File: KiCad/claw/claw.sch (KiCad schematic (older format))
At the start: 15 parts, among them J1 Molex_Spox_3pin, J2 Molex_Spox_3pin, J3 Molex_Spox_3pin, J4 Molex_Spox_3pin, J5 Molex_Spox_3pin, J6 Screw_Terminal_01x02, U1 ESP32_DEVKITV1, U2 TXS0108EPW, U3 74LS241

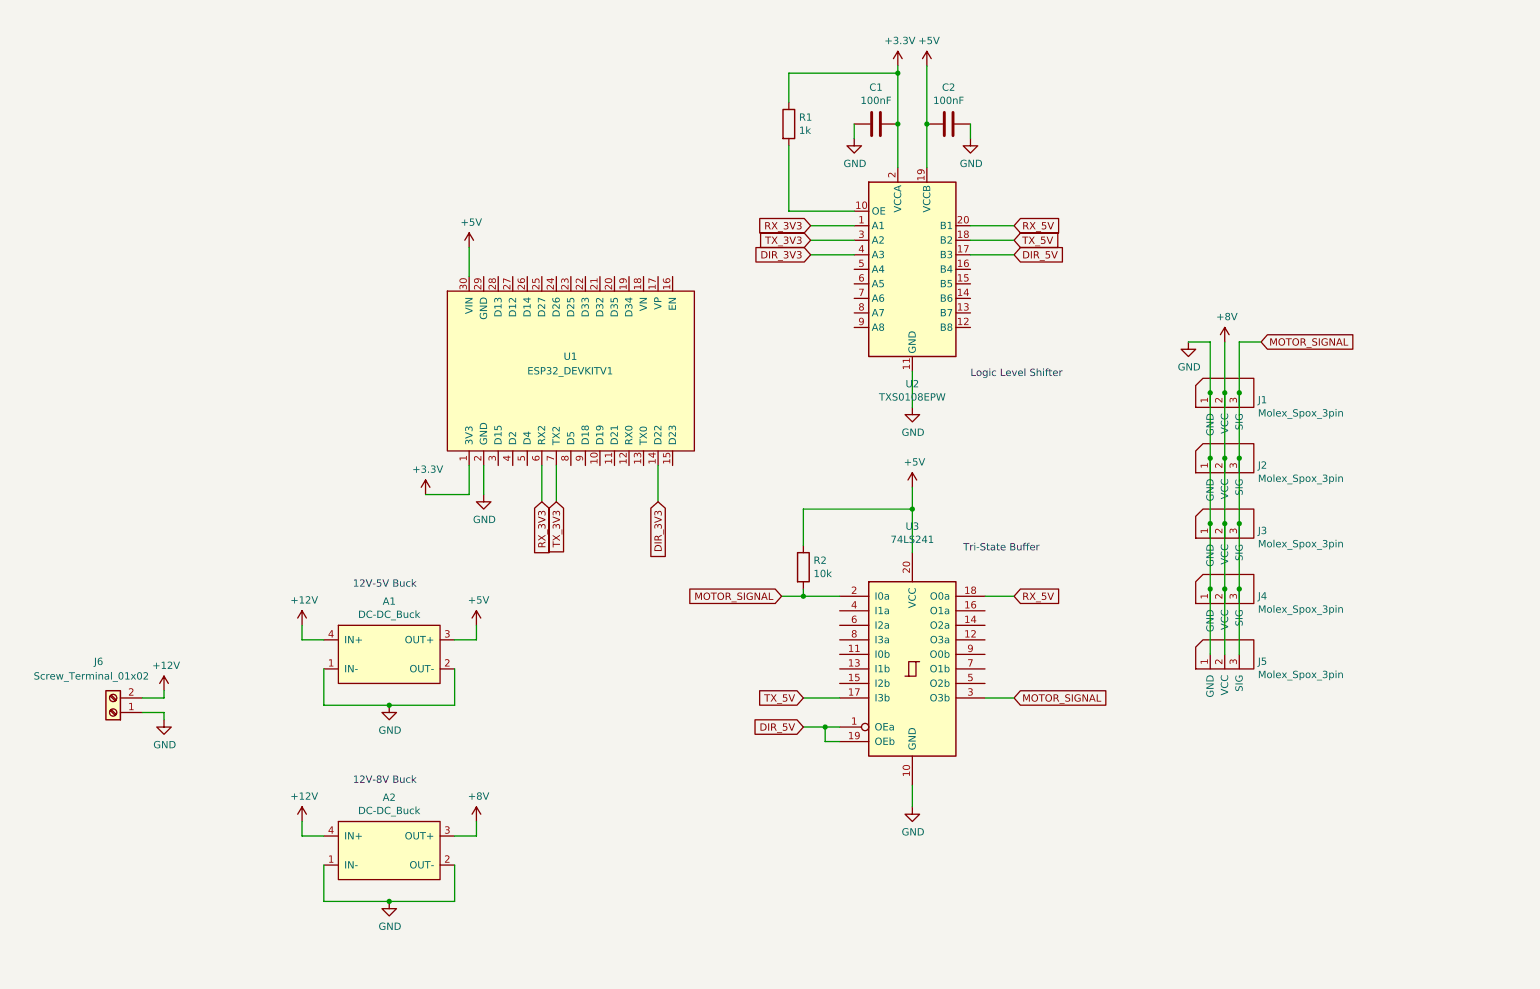
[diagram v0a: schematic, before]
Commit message: added joystick connectors to schematic and layed out components on pcb
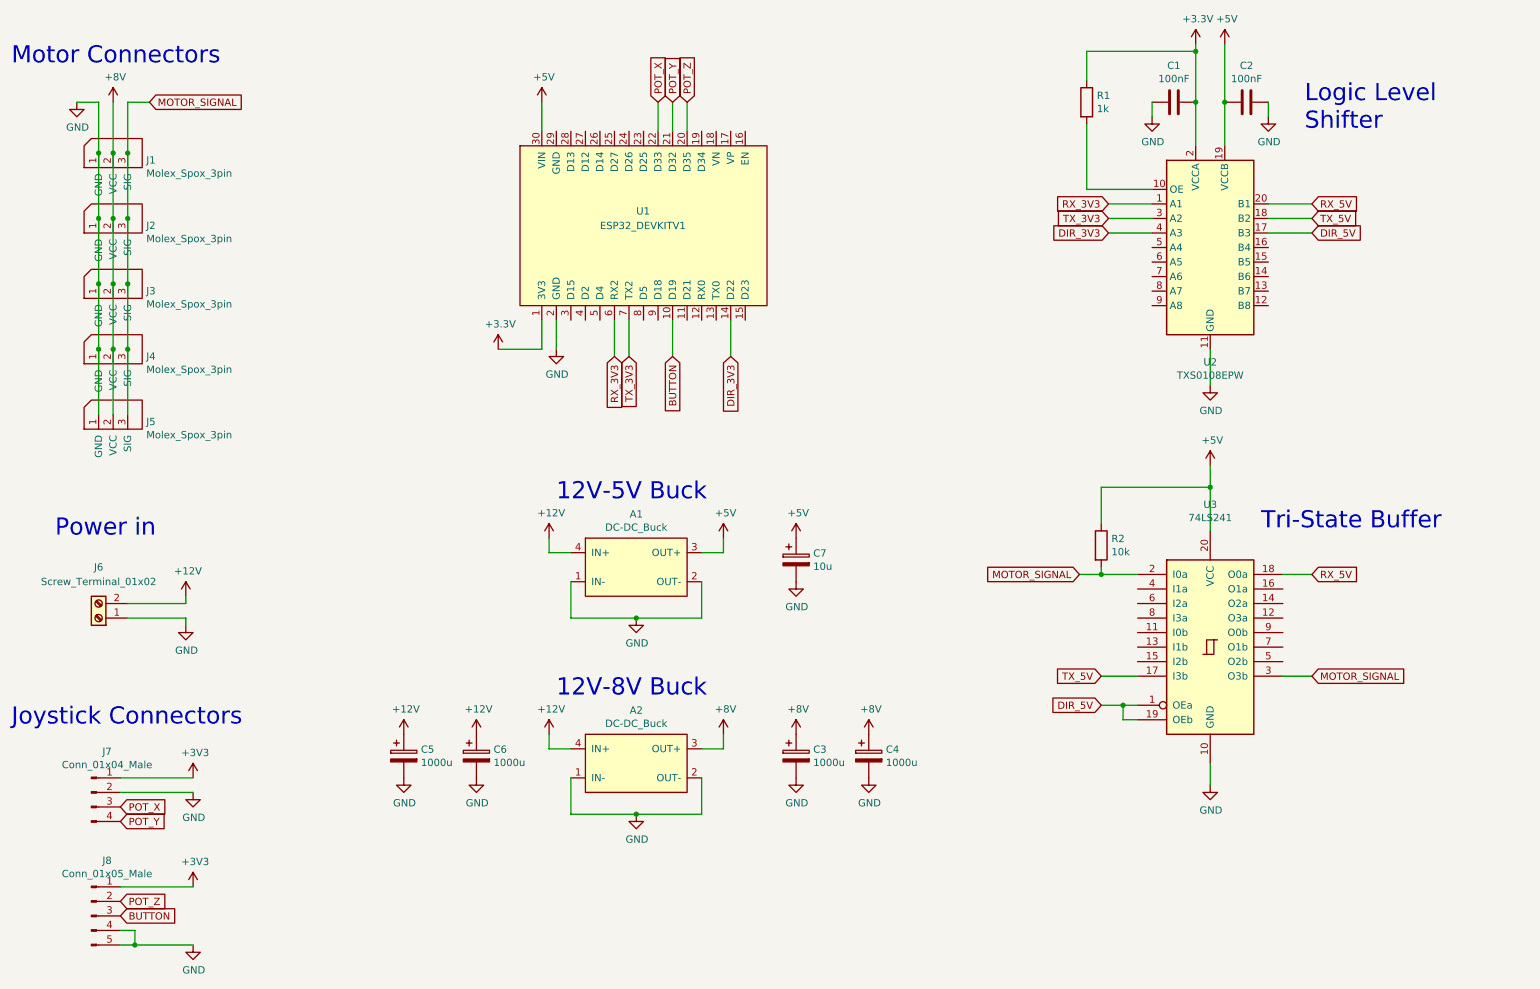
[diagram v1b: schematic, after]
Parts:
- added C3, C4, C5, C6: 1000u, Capacitor_THT:CP_Radial_D10.0mm_P5.00mm, symbol Device:CP
- added C7: 10u, Capacitor_THT:CP_Radial_D4.0mm_P2.00mm, symbol Device:CP
- added J7: Conn_01x04_Male, Connector_JST:JST_PH_B4B-PH-K_1x04_P2.00mm_Vertical, symbol Connector:Conn_01x04_Male
- added J8: Conn_01x05_Male, Connector_JST:JST_PH_B5B-PH-K_1x05_P2.00mm_Vertical, symbol Connector:Conn_01x05_Male
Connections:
- net +12V: now also C5.1, C6.1
- net +3V3: now also J7.1 (Pin_1), J8.1 (Pin_1)
- net +5V: now also C7.1
- net +8V: now also C3.1, C4.1
- net GND: now also C3.2, C4.2, C5.2, C6.2, C7.2, J7.2 (Pin_2), J8.4 (Pin_4), J8.5 (Pin_5)
- net BUTTON: now reaches U1.10 (D19)
- net BUTTON: now also J8.3 (Pin_3)
- net POT_Z: now reaches U1.20 (D35)
- net POT_Z: now also J8.2 (Pin_2)
- net POT_Y: now reaches U1.21 (D32)
- net POT_Y: now also J7.4 (Pin_4)
- net POT_X: now reaches U1.22 (D33)
- net POT_X: now also J7.3 (Pin_3)
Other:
- note added: "Joystick Connectors"
- note added: "Logic Level\nShifter\n"
- note added: "Motor Connectors"
- note added: "Power in"
- note removed: "Logic Level Shifter\n"
- moved on the sheet: A1, A2, C1, C2, J1, J2, J3, J4, J5, J6, R1, R2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

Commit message: pcb traces
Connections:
- net GND: now also U1.29 (GND)
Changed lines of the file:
@@
 Text Notes 1050 4350 0    118  ~ 0
 Power in
+$Comp
+L power:GND #PWR?
+U 1 1 61BD6521
+P 4600 1300
+F 0 "#PWR?" H 4600 1050 50  0001 C CNN
+F 1 "GND" H 4605 1127 50  0000 C CNN
+F 2 "" H 4600 1300 50  0001 C CNN
+F 3 "" H 4600 1300 50  0001 C CNN
+	1    4600 1300
+	1    0    0    -1
+$EndComp
+Wire Wire Line
+	4500 1550 4500 1300
+Wire Wire Line
+	4500 1300 4600 1300
 $EndSCHEMATC
